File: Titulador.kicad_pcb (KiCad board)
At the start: 2 copper layers, 170 x 100 mm, 28 parts, among them J1 1x2_F, J2 1x6_F, J3 1x4_F, J4 1x2_F, J5 1x5_F, J6 1x2_F, J7 1x4_F, Q1 BC548, SW1 SW_DIP_x04, U1 ESP32-DEVKITC-32D, U2 MCU_Friend

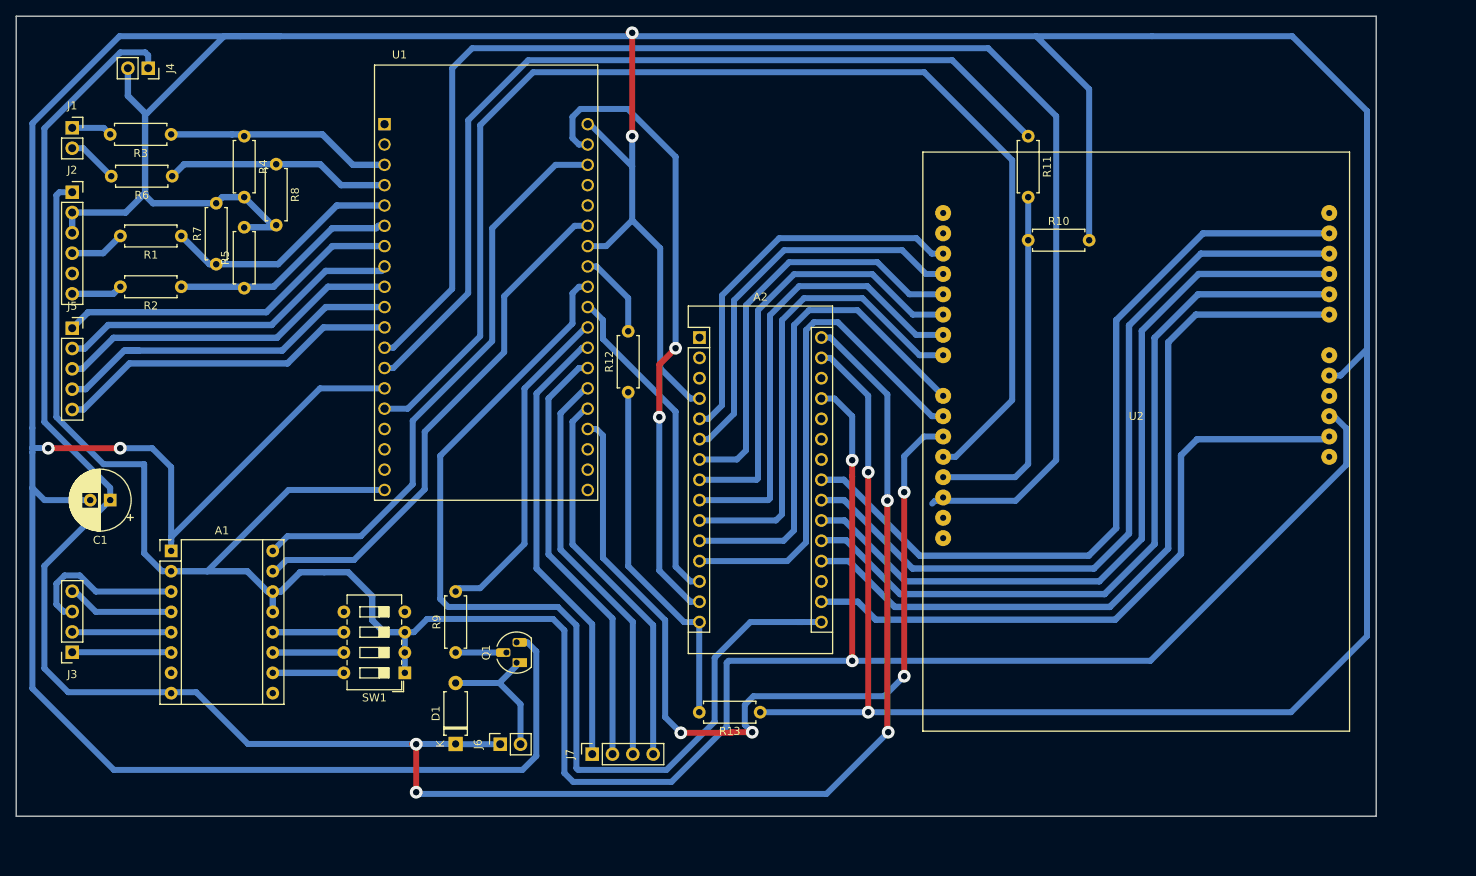
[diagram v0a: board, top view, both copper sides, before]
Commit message: Se actualiza esquematico con atmega328pu
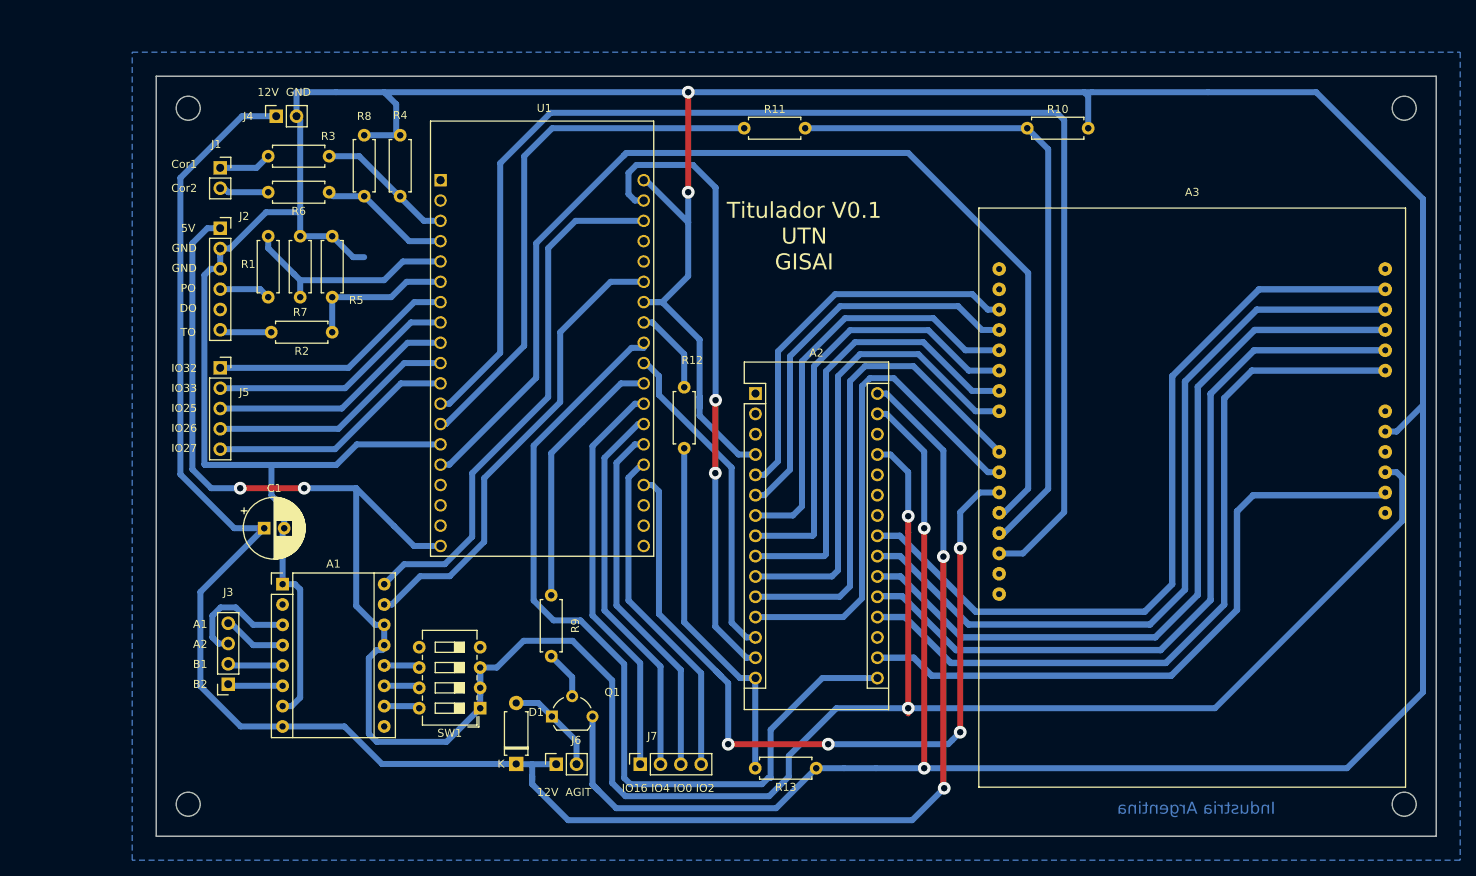
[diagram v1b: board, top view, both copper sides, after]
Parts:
- removed U2: MCU_Friend, pcbTitulador:MCUFriend
- added A3: MCU_Friend, pcbTitulador:MCUFriend, F.Cu at (208.5, 99.5)
- added H1: MountingHole, MountingHole:MountingHole_3mm, F.Cu at (83.0, 54.0)
- added H2: MountingHole, MountingHole:MountingHole_3mm, F.Cu at (235.0, 54.0)
- added H3: MountingHole, MountingHole:MountingHole_3mm, F.Cu at (83.0, 141.0)
- added H4: MountingHole, MountingHole:MountingHole_3mm, F.Cu at (235.0, 141.0)
- A1: value Pololu_Breakout_DRV8825 -> Pololu_DRV8825
- Q1: footprint Package_TO_SOT_THT:TO-92L_HandSolder -> Package_TO_SOT_THT:TO-92L_Wide
- moved R11 35.5 mm to (152.5, 56.5), turned to 0 degrees
- moved R4 20.9 mm to (109.5, 65.0), turned to 90 degrees
- moved R3 19.9 mm to (100.6, 60.0)
- moved J3 19.9 mm to (88.0, 126.0)
- moved R6 19.7 mm to (100.6, 64.5)
- moved R2 19.7 mm to (101.0, 82.0)
- moved C1 19.6 mm to (92.5, 106.5), turned to 0 degrees
- moved J1 19.2 mm to (87.0, 61.5)
- moved J5 19.2 mm to (87.0, 86.5)
- moved J2 19.0 mm to (87.0, 69.0)
- moved J4 17.1 mm to (94.0, 55.0), turned to 90 degrees
- moved A1 14.5 mm to (94.8, 113.5)
- moved R10 14.0 mm to (187.9, 56.5)
- moved R9 12.0 mm to (128.4, 122.5)
- moved R8 11.7 mm to (105.0, 65.0), turned to 90 degrees
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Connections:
- net Agitador renamed /Agitador
- net DirPAP renamed /DirPAP
- net HMISO renamed /HMISO
- net StepPAP renamed /StepPAP
- net VCLK renamed /VCLK
- net VCSO renamed /VCSO
- net VMISO renamed /VMISO
- net VMOSI renamed /VMOSI
- A1 pad 2: +5V -> (no net)
- A1 pad 9: Net-(A1-Pad9) -> (no net)
- A2 pad 1: Net-(A2-Pad1) -> (no net)
- A2 pad 18: Net-(A2-Pad18) -> (no net)
- A2 pad 2: Net-(A2-Pad2) -> (no net)
- A2 pad 24: Net-(A2-Pad24) -> (no net)
- A2 pad 25: Net-(A2-Pad25) -> (no net)
- A2 pad 26: Net-(A2-Pad26) -> (no net)
- A2 pad 28: Net-(A2-Pad28) -> (no net)
- A2 pad 3: Net-(A2-Pad3) -> (no net)
- J2 pad 5: Net-(J2-Pad5) -> (no net)
- SW1 pad 4: Net-(SW1-Pad4) -> (no net)
- SW1 pad 5: Net-(SW1-Pad5) -> (no net)
- U1 pad 1: Net-(U1-Pad1) -> (no net)
- U1 pad 12: HCLK -> /HCLK
- U1 pad 15: HMOSI -> /HMOSI
- U1 pad 16: Net-(U1-Pad16) -> (no net)
- U1 pad 17: Net-(U1-Pad17) -> (no net)
- U1 pad 18: Net-(U1-Pad18) -> (no net)
- U1 pad 2: Net-(U1-Pad2) -> (no net)
- U1 pad 23: Net-(U1-Pad23) -> (no net)
- U1 pad 24: Net-(U1-Pad24) -> (no net)
- U1 pad 35: HCSO -> /HCSO
- U1 pad 36: Net-(U1-Pad36) -> (no net)
- U1 pad 37: Net-(U1-Pad37) -> (no net)
- U1 pad 38: Net-(U1-Pad38) -> (no net)
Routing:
- net HCLK: track 179.9 -> 0.00 mm
- net GND: track 767.4 -> 597.1 mm, vias 6 -> 4
- net /HCLK: track 0.00 -> 166.6 mm
- net HMOSI: track 157.5 -> 0.00 mm
- net /HMOSI: track 0.00 -> 138.0 mm
- net HCSO: track 111.0 -> 0.00 mm, vias 4 -> 0
- net /HCSO: track 0.00 -> 101.2 mm, vias 0 -> 4
- net Net-(R11-Pad1): track 113.0 -> 67.2 mm
- net /HMISO: track 44.7 -> 82.4 mm
- net +12V: track 275.9 -> 248.5 mm, vias 4 -> 2
- net /VCLK: track 127.2 -> 108.6 mm
- net Net-(J5-Pad4): track 44.9 -> 30.9 mm
- net +5V: track 329.4 -> 316.9 mm, vias 2 -> 4
- net Net-(J5-Pad2): track 43.4 -> 30.9 mm
- net Net-(J5-Pad1): track 43.3 -> 30.9 mm
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- added copper zone on B.Cu, net GND
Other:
- board size 170 x 100 mm -> 160 x 95 mm
- board text added: "* Se toman las capacidades de fabricacion nacional, tomando como referencia Mayer SA. *Valores de grilla: Para orden de componentes: 1 mm. Para routeo: 0,5 mm. *Margen general 0,75 mm *Ancho de pista: 0,75 mm *Vías: 1,6 mm / 0,8 mm *Terminaciones: Cu + Flux"
- board text added: "12V AGIT"
- board text added: "12V GND"
- board text added: "5V"
- board text added: "A1"
- board text added: "A2"
- board text added: "B1"
- board text added: "B2"
- board text added: "Cor1"
- board text added: "Cor2"
- board text added: "DO"
- board text added: "GND"
- board text added: "IO16 IO4 IO0 IO2"
- board text added: "IO25"
- board text added: "IO26"
- board text added: "IO27"
- board text added: "IO32"
- board text added: "IO33"
- board text added: "Industria Argentina"
- board text added: "PO"
- board text added: "TO"
- board text added: "Titulador V0.1 UTN GISAI"

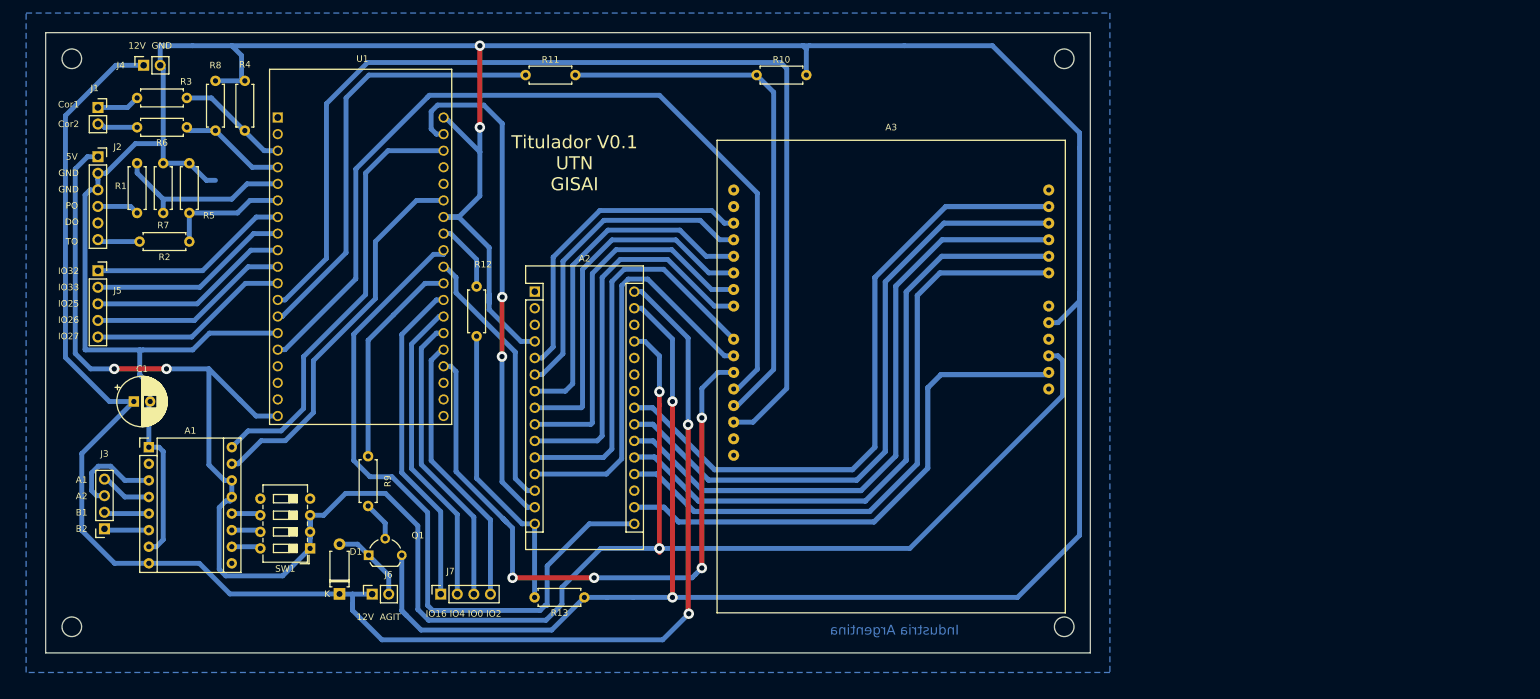
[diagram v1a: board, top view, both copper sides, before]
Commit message: Se finaliza primera version esquematico y PCB
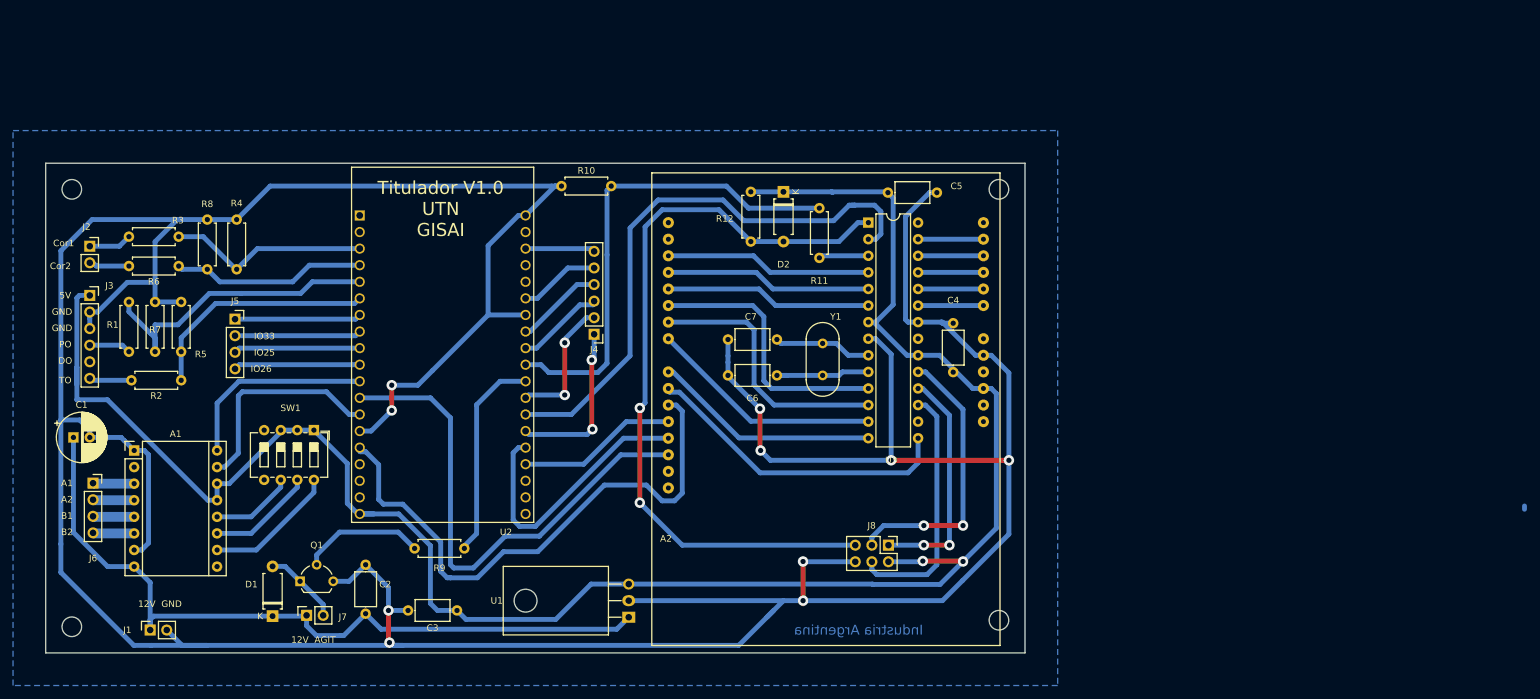
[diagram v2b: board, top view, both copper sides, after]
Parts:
- removed A3: MCU_Friend, pcbTitulador:MCUFriend
- removed the J7 at (139.5, 136.0)
- removed the R10 at (187.9, 56.5)
- removed the R11 at (152.5, 56.5)
- added C2: 0.33uF, Capacitor_THT:C_Axial_L5.1mm_D3.1mm_P7.50mm_Horizontal, F.Cu at (128.0, 139.0)
- added C3: 0.1uF, Capacitor_THT:C_Axial_L5.1mm_D3.1mm_P7.50mm_Horizontal, F.Cu at (142.0, 138.5)
- added C4: 0.1uF, Capacitor_THT:C_Axial_L5.1mm_D3.1mm_P7.50mm_Horizontal, F.Cu at (218.0, 102.0)
- added C5: 0.1uF, Capacitor_THT:C_Axial_L5.1mm_D3.1mm_P7.50mm_Horizontal, F.Cu at (208.0, 74.5)
- added C6: 22nF, Capacitor_THT:C_Axial_L5.1mm_D3.1mm_P7.50mm_Horizontal, F.Cu at (183.5, 102.5)
- added C7: 22nF, Capacitor_THT:C_Axial_L5.1mm_D3.1mm_P7.50mm_Horizontal, F.Cu at (191.0, 97.0)
- added D2: 1N4148, Diode_THT:D_A-405_P7.62mm_Horizontal, F.Cu at (192.0, 74.4)
- added J4: 1x6_F, Connector_PinHeader_2.54mm:PinHeader_1x06_P2.54mm_Vertical, F.Cu at (163.0, 96.2)
- added J8: 2x3_Odd_Even, Connector_PinHeader_2.54mm:PinHeader_2x03_P2.54mm_Vertical, F.Cu at (208.1, 128.5)
- added R12: 10K, Resistor_THT:R_Axial_DIN0207_L6.3mm_D2.5mm_P7.62mm_Horizontal, F.Cu at (187.0, 82.0)
- added U1: LM7805_TO220, Package_TO_SOT_THT:TO-220F-3_Horizontal_TabDown, F.Cu at (168.3, 139.5)
- added U3: ATmega328P-PU, Package_DIP:DIP-28_W7.62mm, F.Cu at (205.0, 79.1)
- added Y1: 16MHz, Crystal:Crystal_HC18-U_Vertical, F.Cu at (198.0, 97.6)
- A2: value Arduino_Nano_v3.x -> MCU_Friend; footprint Module:Arduino_Nano -> pcbTitulador:MCUFriend
- J5: value 1x5_F -> 1x4_F; footprint Connector_PinSocket_2.54mm:PinSocket_1x05_P2.54mm_Vertical -> Connector_PinSocket_2.54mm:PinSocket_1x04_P2.54mm_Vertical
- R10: renamed from R13; value 27K -> 33K
- R4, R5, R7, R8: value 27K -> 33K
- moved J1 86.5 mm to (95.0, 141.5)
- moved R10 63.1 mm to (158.0, 73.5), turned to 0 degrees
- moved R11 53.9 mm to (197.5, 84.5)
- moved A2 47.0 mm to (198.5, 104.5)
- moved H2 22.4 mm to (225.0, 74.0)
- moved J5 22.3 mm to (108.0, 93.9)
- moved J3 21.3 mm to (85.8, 90.2)
- moved R1 21.3 mm to (91.8, 91.2)
- moved R2 21.3 mm to (99.8, 103.2)
- moved R3 21.3 mm to (99.4, 81.2)
- moved R4 21.3 mm to (108.2, 86.2)
- moved R5 21.3 mm to (99.8, 98.9)
- moved R6 21.3 mm to (99.4, 85.8)
- moved R7 21.3 mm to (95.8, 98.9)
- moved R8 21.3 mm to (103.8, 86.2)
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- renumbered J4 to J1, J1 to J2, J2 to J3, J3 to J6, J6 to J7, R12 to R11, U1 to U2
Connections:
- A2 pad 11: Net-(A2-Pad11) -> /HCSO
- A2 pad 12: Net-(A2-Pad12) -> /HMOSI
- A2 pad 13: /VCSO -> /HMISO
- A2 pad 14: /VMOSI -> /HCLK
- A2 pad 15: /VMISO -> (no net)
- A2 pad 16: /VCLK -> (no net)
- A2 pad 17: +3V3 -> (no net)
- A2 pad 18: (no net) -> Net-(A2-Pad18)
- A2 pad 23: Net-(A2-Pad23) -> (no net)
- A2 pad 24: (no net) -> GND
- A2 pad 26: (no net) -> +5V
- A2 pad 27: +5V -> (no net)
- A2 pad 3: (no net) -> Net-(A2-Pad3)
- A2 pad 4: GND -> Net-(A2-Pad4)
- J6 pad 1: Net-(A1-Pad6) -> Net-(A1-Pad3)
- J6 pad 2: Net-(A1-Pad5) -> Net-(A1-Pad4)
- J6 pad 3: Net-(A1-Pad3) -> Net-(A1-Pad5)
- J6 pad 4: Net-(A1-Pad4) -> Net-(A1-Pad6)
- R10 pad 2: /VMISO -> Net-(R10-Pad2)
- R11 pad 1: /VMISO -> Net-(R11-Pad1)
- R11 pad 2: Net-(R12-Pad2) -> Net-(R10-Pad2)
- U2 pad 11: Net-(J5-Pad5) -> /DirPAP
- U2 pad 13: Net-(R11-Pad1) -> /StepPAP
- U2 pad 15: /HMOSI -> /HCSO
- U2 pad 21: /VMOSI -> (no net)
- U2 pad 22: /DirPAP -> Net-(J4-Pad6)
- U2 pad 25: /StepPAP -> Net-(J4-Pad5)
- U2 pad 27: Net-(R12-Pad2) -> Net-(J4-Pad4)
- U2 pad 28: /VCLK -> Net-(J4-Pad3)
- U2 pad 29: /VCSO -> Net-(R10-Pad2)
- U2 pad 34: Net-(J7-Pad4) -> /HMISO
- U2 pad 35: /HCSO -> /HMOSI
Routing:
- net +12V: track 248.5 -> 117.3 mm, vias 2 -> 0
- net Net-(D2-Pad2): track 0.00 -> 116.8 mm, vias 0 -> 2
- net /HMOSI: track 138.0 -> 25.0 mm
- net /VCLK: track 108.6 -> 0.00 mm
- net Net-(A2-Pad23): track 99.3 -> 0.00 mm
- net Net-(A2-Pad22): track 98.6 -> 10.0 mm
- net /HCLK: track 166.6 -> 78.4 mm
- net Net-(A2-Pad21): track 97.8 -> 10.0 mm
- net Net-(A2-Pad20): track 96.9 -> 10.0 mm
- net Net-(A2-Pad19): track 96.1 -> 10.3 mm
- net +3V3: track 81.3 -> 0.00 mm
- net /VMOSI: track 78.9 -> 0.00 mm, vias 2 -> 0
- net Net-(R10-Pad2): track 0.00 -> 74.3 mm
- net Net-(A2-Pad12): track 63.2 -> 0.00 mm
- net Net-(A2-Pad11): track 61.9 -> 0.00 mm
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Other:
- board size 160 x 95 mm -> 150 x 75 mm
- board text added: "*Valores de grilla: Para orden de componentes: 1 mm. Para routeo: 0,5 mm. *Margen general 0,75 mm *Ancho de pista: 0,75 mm *Vías: 1,6 mm / 0,8 mm *Terminaciones: Cu + Flux"
- board text added: "Titulador V1.0 UTN GISAI"
- board text removed: "* Se toman las capacidades de fabricacion nacional, tomando como referencia Mayer SA. *Valores de grilla: Para orden de componentes: 1 mm. Para routeo: 0,5 mm. *Margen general 0,75 mm *Ancho de pista: 0,75 mm *Vías: 1,6 mm / 0,8 mm *Terminaciones: Cu + Flux"
- board text removed: "IO16 IO4 IO0 IO2"
- board text removed: "IO27"
- board text removed: "IO32"
- board text removed: "Titulador V0.1 UTN GISAI"

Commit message: Correcciones menores
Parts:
- moved Q1 5.04 mm to (118.0, 129.0)
- moved J7 2.30 mm to (119.5, 137.0)
- moved C3 1.58 mm to (142.5, 137.0)
- moved J1 1.50 mm to (95.0, 140.0)
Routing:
- net GND: track 630.5 -> 765.8 mm
- net /HCLK: track 78.4 -> 73.6 mm
- net Net-(D1-Pad2): track 11.8 -> 15.0 mm
- net Net-(Q1-Pad2): track 19.0 -> 16.0 mm
- net /HCSO: track 86.6 -> 89.3 mm
- net +5V: track 301.5 -> 299.6 mm
- net +12V: track 117.3 -> 116.7 mm
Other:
- board text added: "IO04"
- board text added: "IO18"
- board text added: "IO19"
- board text added: "IO21"
- board text added: "IO22"
- board text added: "IO32"
- board text added: "Titulador V1.0 UTN FRSFCO GISAI AÑO 2021"
- board text added: "UTN FRSFCO -- Industria Argentina"
- board text removed: "Industria Argentina"
- board text removed: "Titulador V1.0 UTN GISAI"
